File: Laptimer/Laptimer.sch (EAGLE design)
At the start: 68 parts, among them IC1 MCP73831/OT, IC2 MAX631CPA, IC5 NE555D, Q4 PBSS4120T, X1 mini-usb, X2 332-02

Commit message: started redoing the layout for the new alu housing
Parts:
- removed H1, H2, H3, H4: MOUNT-HOLE3.0, holes:MOUNT-HOLE3.0
- removed IC2: MAX631CPA, maxim:MAX631CPA
- removed U$21: APC220, APC220:APC220
- added C9: (no value), microbuilder:CAP_CERAMIC_0805MP
- added D1: MBRA140, SparkFun-DiscreteSemi:MBRA140
- added XB1, XB2: XBEE-PRO, microbuilder:XBEE-PRO
- C2: value 100nf -> 100n; device rcl:C-EU050-025X075 -> microbuilder:CAP_CERAMIC_0603MP
- L1: value 330u -> MSS1038-473MLC 47u; device rcl:L-EU0204/7 -> SparkFun-Passives:INDUCTORPWR
- Q1: value (none) -> 8mhz
- U$2: value APC220 -> AP1509; device APC220:APC220 -> unicorn_v2:AP1509
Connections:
- removed net 5.0V: C16.1, C19.1, C2.1, D2.C, FB1.P$1, IC2.VOUT, IC5.R, IC5.V+, MCU.AVCC, MCU.UVCC, MCU.VCC, MCU.VCC1, Q4.C, R18.1, R22.1, U$2.VCC, U$21.VCC
- removed net N$37: L1.2, PWR-SW.1
- new net 3.3V: C16.1, C19.1, C9.P$1, D2.C, FB1.P$1, IC5.R, IC5.V+, L1.1, MCU.AVCC, MCU.UVCC, MCU.VCC, MCU.VCC1, Q4.C, R18.1, R22.1, U$2.FB
- new net N$17: D1.C, L1.2, U$2.OUT
- new net VBAT: C2.P$1, PWR-SW.1, U$2.VIN
- net +UB: no longer IC1.VDD, MCU.VBUS, U$1.4
- net GND: now also C2.P$2, C9.P$2, D1.A, U$2.GND1, U$2.GND2, U$2.GND3, U$2.GND4, U$2.SD; no longer C2.2, IC2.GND, IC2.LBI, IC2.VFB, U$2.GND, U$21.GND
- net N$14: now also IC1.VDD, U$1.4; no longer IC2.LX, L1.1
- net RX1: now also XB2.DOUT; no longer U$2.TXD
- net RX2: now also XB1.DOUT; no longer U$21.TXD
- net TX1: now also XB2.DIN/!CONFIG; no longer U$2.RXD
- net TX2: now also XB1.DIN/!CONFIG; no longer U$21.RXD
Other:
- moved on the sheet: C2

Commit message: added 5-way CAN splitter and continued work
more work have been done one the laptimer layout
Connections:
- removed net N$14: IC1.VDD, U$1.4
- net +UB: now also IC1.VDD, U$1.4
- net 3.3V: now also XB1.!RESET, XB1.VCC, XB2.!RESET, XB2.VCC
- net GND: now also XB1.GND, XB2.GND
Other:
- moved on the sheet: S2
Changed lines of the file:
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@@
 <part name="U$3" library="microbuilder" deviceset="3.3V" device=""/>
 <part name="U$15" library="microbuilder" deviceset="3.3V" device=""/>
+<part name="SUPPLY1" library="supply2" deviceset="+UB" device=""/>
+<part name="U$16" library="microbuilder" deviceset="3.3V" device=""/>
+<part name="U$17" library="microbuilder" deviceset="3.3V" device=""/>
+<part name="GND5" library="supply1" deviceset="GND" device=""/>
+<part name="GND7" library="supply1" deviceset="GND" device=""/>
 </parts>
 <sheets>
@@
 <wire x1="53.34" y1="198.12" x2="99.06" y2="198.12" width="0.1524" layer="97"/>
 <wire x1="99.06" y1="198.12" x2="99.06" y2="157.48" width="0.1524" layer="97"/>
-<wire x1="200.66" y1="157.48" x2="198.12" y2="236.22" width="0.1524" layer="97"/>
-<wire x1="198.12" y1="236.22" x2="142.24" y2="236.22" width="0.1524" layer="97"/>
+<wire x1="200.66" y1="157.48" x2="200.66" y2="236.22" width="0.1524" layer="97"/>
+<wire x1="200.66" y1="236.22" x2="142.24" y2="236.22" width="0.1524" layer="97"/>
 <wire x1="142.24" y1="236.22" x2="142.24" y2="157.48" width="0.1524" layer="97"/>
 <wire x1="142.24" y1="236.22" x2="99.06" y2="236.22" width="0.1524" layer="97"/>
@@
 <instance part="C19" gate="G$1" x="53.34" y="144.78"/>
 <instance part="D2" gate="G$1" x="27.94" y="142.24" rot="R90"/>
-<instance part="GND15" gate="1" x="12.7" y="132.08"/>
+<instance part="GND15" gate="1" x="12.7" y="129.54"/>
 <instance part="GND26" gate="1" x="45.72" y="137.16"/>
 <instance part="GND27" gate="1" x="53.34" y="137.16"/>
@@
 <instance part="R5" gate="G$1" x="73.66" y="210.82" rot="R270"/>
 <instance part="JP2" gate="G$1" x="160.02" y="139.7"/>
-<instance part="S2" gate="G$1" x="20.32" y="137.16"/>
+<instance part="S2" gate="G$1" x="20.32" y="134.62"/>
 <instance part="FB1" gate="G$1" x="22.86" y="111.76" rot="R270"/>
 <instance part="C1" gate="G$1" x="17.78" y="81.28"/>
@@
 <instance part="U$3" gate="G$1" x="83.82" y="231.14"/>
 <instance part="U$15" gate="G$1" x="170.18" y="220.98"/>
+<instance part="SUPPLY1" gate="G$1" x="27.94" y="30.48"/>
+<instance part="U$16" gate="G$1" x="254" y="223.52"/>
+<instance part="U$17" gate="G$1" x="254" y="154.94"/>
+<instance part="GND5" gate="1" x="254" y="160.02"/>
+<instance part="GND7" gate="1" x="254" y="91.44"/>
 </instances>
 <busses>
@@
 <segment>
 <pinref part="GND15" gate="1" pin="GND"/>
-<wire x1="15.24" y1="137.16" x2="12.7" y2="137.16" width="0.1524" layer="91"/>
-<wire x1="12.7" y1="137.16" x2="12.7" y2="134.62" width="0.1524" layer="91"/>
+<wire x1="15.24" y1="134.62" x2="12.7" y2="134.62" width="0.1524" layer="91"/>
+<wire x1="12.7" y1="134.62" x2="12.7" y2="132.08" width="0.1524" layer="91"/>
 <pinref part="S2" gate="G$1" pin="1"/>
 </segment>
@@
 <pinref part="U$9" gate="G$1" pin="GND"/>
 </segment>
+<segment>
+<pinref part="XB2" gate="G$1" pin="GND"/>
+<pinref part="GND7" gate="1" pin="GND"/>
+<wire x1="256.54" y1="96.52" x2="254" y2="96.52" width="0.1524" layer="91"/>
+<wire x1="254" y1="96.52" x2="254" y2="93.98" width="0.1524" layer="91"/>
+</segment>
+<segment>
+<pinref part="XB1" gate="G$1" pin="GND"/>
+<pinref part="GND5" gate="1" pin="GND"/>
+<wire x1="256.54" y1="165.1" x2="254" y2="165.1" width="0.1524" layer="91"/>
+<wire x1="254" y1="165.1" x2="254" y2="162.56" width="0.1524" layer="91"/>
+</segment>
 </net>
 <net name="XTAL2" class="0">
@@
 <junction x="27.94" y="129.54"/>
 <pinref part="D2" gate="G$1" pin="A"/>
-<wire x1="27.94" y1="134.62" x2="27.94" y2="137.16" width="0.1524" layer="91"/>
 <junction x="27.94" y="134.62"/>
 <pinref part="R22" gate="G$1" pin="2"/>
-<wire x1="27.94" y1="137.16" x2="27.94" y2="139.7" width="0.1524" layer="91"/>
+<wire x1="27.94" y1="134.62" x2="27.94" y2="139.7" width="0.1524" layer="91"/>
 <wire x1="27.94" y1="134.62" x2="35.56" y2="134.62" width="0.1524" layer="91"/>
 <wire x1="35.56" y1="134.62" x2="35.56" y2="137.16" width="0.1524" layer="91"/>
 <junction x="27.94" y="134.62"/>
-<wire x1="25.4" y1="137.16" x2="27.94" y2="137.16" width="0.1524" layer="91"/>
-<junction x="27.94" y="137.16"/>
+<wire x1="25.4" y1="134.62" x2="27.94" y2="134.62" width="0.1524" layer="91"/>
+<junction x="27.94" y="134.62"/>
 <pinref part="S2" gate="G$1" pin="2"/>
 </segment>
@@
 <junction x="88.9" y="182.88"/>
 </segment>
+<segment>
+<pinref part="U$1" gate="G$1" pin="4"/>
+<pinref part="IC1" gate="G$1" pin="VDD"/>
+<wire x1="12.7" y1="27.94" x2="27.94" y2="27.94" width="0.1524" layer="91"/>
+<pinref part="SUPPLY1" gate="G$1" pin="+UB"/>
+<wire x1="27.94" y1="27.94" x2="38.1" y2="27.94" width="0.1524" layer="91"/>
+<junction x="27.94" y="27.94"/>
+</segment>
 </net>
 <net name="PT-IN" class="0">
@@
 <pinref part="U$15" gate="G$1" pin="3.3V"/>
 </segment>
+<segment>
+<pinref part="XB2" gate="G$1" pin="VCC"/>
+<pinref part="U$17" gate="G$1" pin="3.3V"/>
+<wire x1="256.54" y1="149.86" x2="254" y2="149.86" width="0.1524" layer="91"/>
+<wire x1="254" y1="149.86" x2="254" y2="152.4" width="0.1524" layer="91"/>
+<pinref part="XB2" gate="G$1" pin="!RESET"/>
+<wire x1="256.54" y1="147.32" x2="254" y2="147.32" width="0.1524" layer="91"/>
+<wire x1="254" y1="147.32" x2="254" y2="149.86" width="0.1524" layer="91"/>
+<junction x="254" y="149.86"/>
+</segment>
+<segment>
+<pinref part="XB1" gate="G$1" pin="VCC"/>
+<pinref part="U$16" gate="G$1" pin="3.3V"/>
+<wire x1="256.54" y1="218.44" x2="254" y2="218.44" width="0.1524" layer="91"/>
+<wire x1="254" y1="218.44" x2="254" y2="220.98" width="0.1524" layer="91"/>
+<pinref part="XB1" gate="G$1" pin="!RESET"/>
+<wire x1="256.54" y1="215.9" x2="254" y2="215.9" width="0.1524" layer="91"/>
+<wire x1="254" y1="215.9" x2="254" y2="218.44" width="0.1524" layer="91"/>
+<junction x="254" y="218.44"/>
+</segment>
 </net>
 <net name="VBAT" class="0">
@@
 </segment>
 </net>
-<net name="N$14" class="0">
-<segment>
-<pinref part="U$1" gate="G$1" pin="4"/>
-<pinref part="IC1" gate="G$1" pin="VDD"/>
-<wire x1="12.7" y1="27.94" x2="38.1" y2="27.94" width="0.1524" layer="91"/>
-</segment>
-</net>

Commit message: continued work on the layout
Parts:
- removed LED10, LED11, LED12, LED13, LED14, LED15, LED16: SFH 309, adafruit:LED3MM
- removed PWR-SW: (no value), adafruit:JST_2PIN-SMT-RA
- removed SYS-STATUS: M04, unicorn_v2:M04
- removed X2: 332-02, con-garry:332-02
- added C10, C11: 10u, microbuilder:CAP_CERAMIC_0805MP
- added JP3: (no value), adafruit:PINHD-1X3
- added R7: 220, rcl:R-EU_R0603
- added S1: (no value), switch:LPV-1
- added U$18, U$19: BI-LEVEL-LED-INDICATOR, unicorn_v2:BI-LEVEL-LED-INDICATOR
- JP1: device unicorn_v2:M03 -> adafruit:PINHD-1X3
- JP2: device unicorn_v2:M03 -> microbuilder:HEADER-1X2ROUND
- U$1: value M04 -> BI-LEVEL-LED-INDICATOR; device unicorn_v2:M04 -> unicorn_v2:BI-LEVEL-LED-INDICATOR
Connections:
- removed net CHARGING-LED: R2.1, U$1.3
- new net N$14: R2.1, U$1.CATHODE1
- new net N$15: R7.2, U$18.ANODE1
- net +UB: now also C10.P$2, U$1.ANODE1; no longer U$1.4
- net 3.3V: now also R16.1
- net CHRG-DONE-LED: now also U$1.ANODE2; no longer U$1.2
- net GND: now also C10.P$1, C11.P$2, S1.B, S1.B1, U$1.CATHODE2, U$18.CATHODE1, U$18.CATHODE2, U$19.CATHODE1, U$19.CATHODE2; no longer SYS-STATUS.4, U$1.1
- net INT: now also JP3.2; no longer JP2.2, LED10.C, LED11.C, LED12.C, LED13.C, LED14.C, LED15.C, LED16.C
- net LED1: now also R7.1; no longer R16.1
- net LED2: now also R14.1; no longer R15.1
- net LED3: now also R15.1; no longer R14.1
- net N$10: now also JP2.1, JP3.1; no longer JP2.3, X2-2.S
- net N$21: now also U$18.ANODE2; no longer SYS-STATUS.3
- net N$25: now also U$19.ANODE1; no longer SYS-STATUS.2
- net N$31: now also C11.P$1, S1.P; no longer PWR-SW.2
- net N$32: now also U$19.ANODE2; no longer SYS-STATUS.1
- net N$40: now also JP2.2, JP3.3; no longer JP2.1, LED10.A, LED11.A, LED12.A, LED13.A, LED14.A, LED15.A, LED16.A, X2-1.S
- net VBAT: now also S1.O; no longer PWR-SW.1
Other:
- note added: "SPI interface"
- note added: "XBee interface"
- note removed: "APC RF interface"
- moved on the sheet: BATTERY, C2, C4, C8, C9, D1, L1, PTC1, R14, R15, R16, R5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

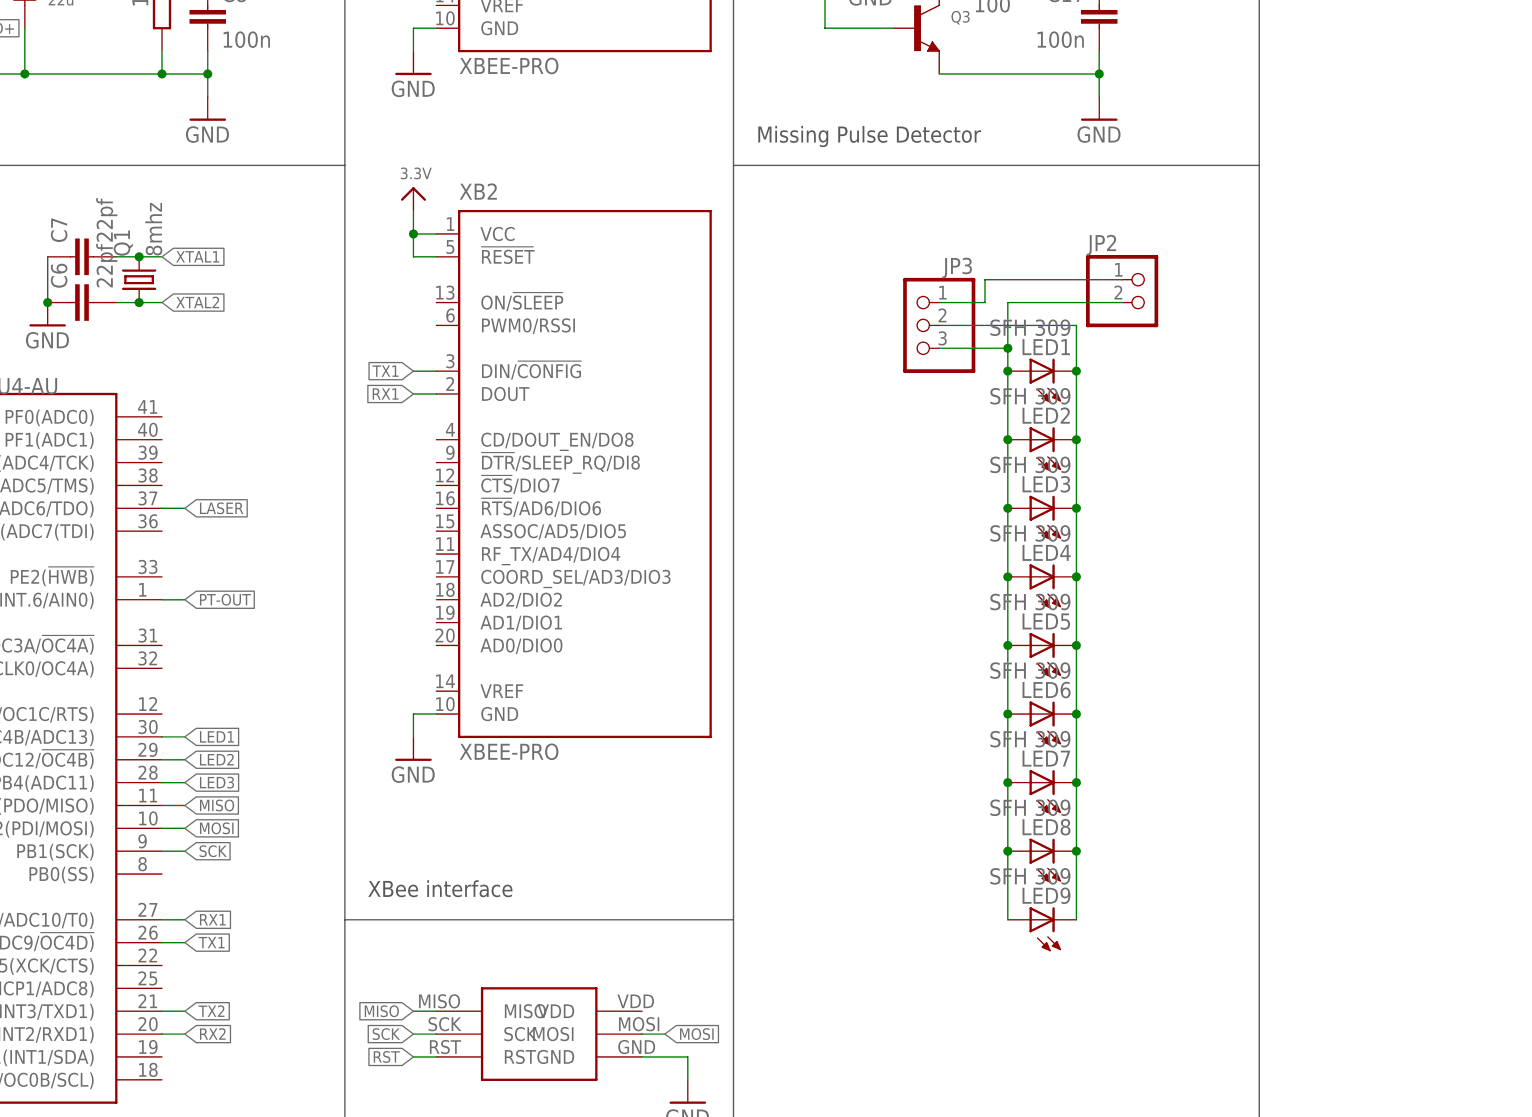
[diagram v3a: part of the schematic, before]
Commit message: removed second xbee
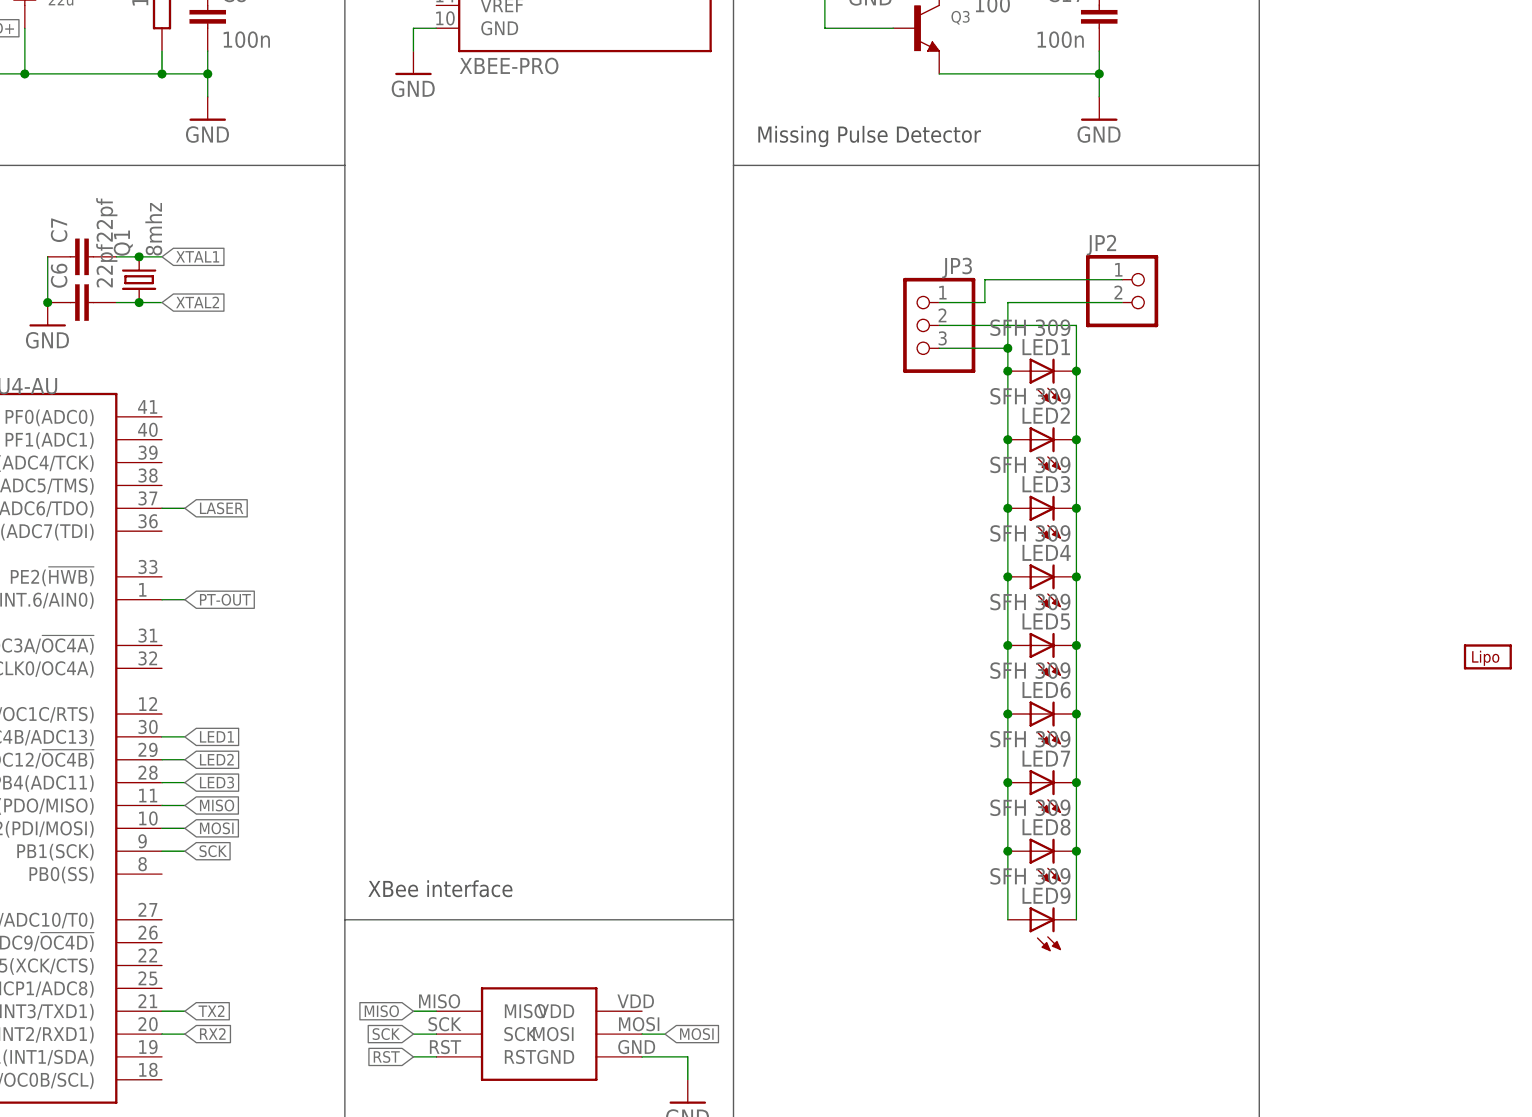
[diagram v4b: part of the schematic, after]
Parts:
- removed XB2: XBEE-PRO, microbuilder:XBEE-PRO
- added U$17: LIPO-OUTLINE2000, SparkFun-Electromechanical:LIPO-OUTLINE2000
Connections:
- removed net RX1: MCU.PD7(OC4D/ADC10/T0), XB2.DOUT
- removed net TX1: MCU.PD6(T1/ADC9/!OC4D), XB2.DIN/!CONFIG
- net 3.3V: no longer XB2.!RESET, XB2.VCC
- net GND: no longer XB2.GND
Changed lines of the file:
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@@
 <part name="C8" library="rcl" deviceset="C-EU" device="C0603K" value="100n"/>
 <part name="XB1" library="microbuilder" deviceset="XBEE" device="-PRO"/>
-<part name="XB2" library="microbuilder" deviceset="XBEE" device="-PRO"/>
 <part name="U$2" library="unicorn_v2" deviceset="AP1509" device=""/>
 <part name="C2" library="microbuilder" deviceset="CAP_CERAMIC" device="_0603MP" value="100n"/>
@@
 <part name="SUPPLY1" library="supply2" deviceset="+UB" device=""/>
 <part name="U$16" library="microbuilder" deviceset="3.3V" device=""/>
-<part name="U$17" library="microbuilder" deviceset="3.3V" device=""/>
 <part name="GND5" library="supply1" deviceset="GND" device=""/>
-<part name="GND7" library="supply1" deviceset="GND" device=""/>
 <part name="GND3" library="supply1" deviceset="GND" device=""/>
 <part name="C10" library="microbuilder" deviceset="CAP_CERAMIC" device="_0805MP" value="10u"/>
@@
 <part name="JP2" library="microbuilder" deviceset="HEADER-1X2" device="ROUND"/>
 <part name="JP1" library="adafruit" deviceset="PINHD-1X3" device=""/>
+<part name="U$17" library="SparkFun-Electromechanical" deviceset="LIPO-OUTLINE" device="2000"/>
 </parts>
 <sheets>
@@
 <instance part="C8" gate="G$1" x="83.82" y="175.26"/>
 <instance part="XB1" gate="G$1" x="124.46" y="200.66"/>
-<instance part="XB2" gate="G$1" x="124.46" y="124.46"/>
 <instance part="U$2" gate="G$1" x="177.8" y="20.32"/>
 <instance part="C2" gate="G$1" x="154.94" y="10.16"/>
@@
 <instance part="SUPPLY1" gate="G$1" x="22.86" y="30.48"/>
 <instance part="U$16" gate="G$1" x="106.68" y="231.14"/>
-<instance part="U$17" gate="G$1" x="106.68" y="154.94"/>
 <instance part="GND5" gate="1" x="106.68" y="167.64"/>
-<instance part="GND7" gate="1" x="106.68" y="91.44"/>
 <instance part="GND3" gate="1" x="12.7" y="7.62"/>
 <instance part="C10" gate="G$1" x="12.7" y="20.32" rot="R180"/>
@@
 <instance part="JP2" gate="G$1" x="187.96" y="142.24"/>
 <instance part="JP1" gate="A" x="93.98" y="210.82"/>
+<instance part="U$17" gate="G$1" x="223.52" y="101.6"/>
 </instances>
 <busses>
@@
 </segment>
 <segment>
-<pinref part="XB2" gate="G$1" pin="GND"/>
-<pinref part="GND7" gate="1" pin="GND"/>
-<wire x1="109.22" y1="96.52" x2="106.68" y2="96.52" width="0.1524" layer="91"/>
-<wire x1="106.68" y1="96.52" x2="106.68" y2="93.98" width="0.1524" layer="91"/>
-</segment>
-<segment>
 <pinref part="XB1" gate="G$1" pin="GND"/>
 <pinref part="GND5" gate="1" pin="GND"/>
@@
 <wire x1="27.94" y1="83.82" x2="27.94" y2="86.36" width="0.1524" layer="91"/>
 <label x="27.94" y="86.36" size="1.27" layer="95" rot="R180" xref="yes"/>
-</segment>
-</net>
-<net name="RX1" class="0">
-<segment>
-<wire x1="106.68" y1="132.08" x2="109.22" y2="132.08" width="0.1524" layer="91"/>
-<label x="106.68" y="132.08" size="1.27" layer="95" rot="R180" xref="yes"/>
-<pinref part="XB2" gate="G$1" pin="DOUT"/>
-</segment>
-<segment>
-<pinref part="MCU" gate="G$1" pin="PD7(OC4D/ADC10/T0)"/>
-<wire x1="78.74" y1="73.66" x2="81.28" y2="73.66" width="0.1524" layer="91"/>
-<label x="81.28" y="73.66" size="1.27" layer="95" xref="yes"/>
-</segment>
-</net>
-<net name="TX1" class="0">
-<segment>
-<wire x1="106.68" y1="134.62" x2="109.22" y2="134.62" width="0.1524" layer="91"/>
-<label x="106.68" y="134.62" size="1.27" layer="95" rot="R180" xref="yes"/>
-<pinref part="XB2" gate="G$1" pin="DIN/!CONFIG"/>
-</segment>
-<segment>
-<pinref part="MCU" gate="G$1" pin="PD6(T1/ADC9/!OC4D)"/>
-<wire x1="78.74" y1="71.12" x2="81.28" y2="71.12" width="0.1524" layer="91"/>
-<label x="81.28" y="71.12" size="1.27" layer="95" xref="yes"/>
 </segment>
 </net>
@@
 </segment>
 <segment>
-<pinref part="XB2" gate="G$1" pin="VCC"/>
-<pinref part="U$17" gate="G$1" pin="3.3V"/>
-<wire x1="109.22" y1="149.86" x2="106.68" y2="149.86" width="0.1524" layer="91"/>
-<wire x1="106.68" y1="149.86" x2="106.68" y2="152.4" width="0.1524" layer="91"/>
-<pinref part="XB2" gate="G$1" pin="!RESET"/>
-<wire x1="109.22" y1="147.32" x2="106.68" y2="147.32" width="0.1524" layer="91"/>
-<wire x1="106.68" y1="147.32" x2="106.68" y2="149.86" width="0.1524" layer="91"/>
-<junction x="106.68" y="149.86"/>
-</segment>
-<segment>
